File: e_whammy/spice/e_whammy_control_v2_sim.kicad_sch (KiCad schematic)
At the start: 29 parts, among them Q1 2N7002, U1 ${SIM.PARAMS}, U2 ${SIM.PARAMS}, U3 ADG779, U4 OPEN_COLLECTOR_COMPARATOR, U5 OPEN_COLLECTOR_COMPARATOR

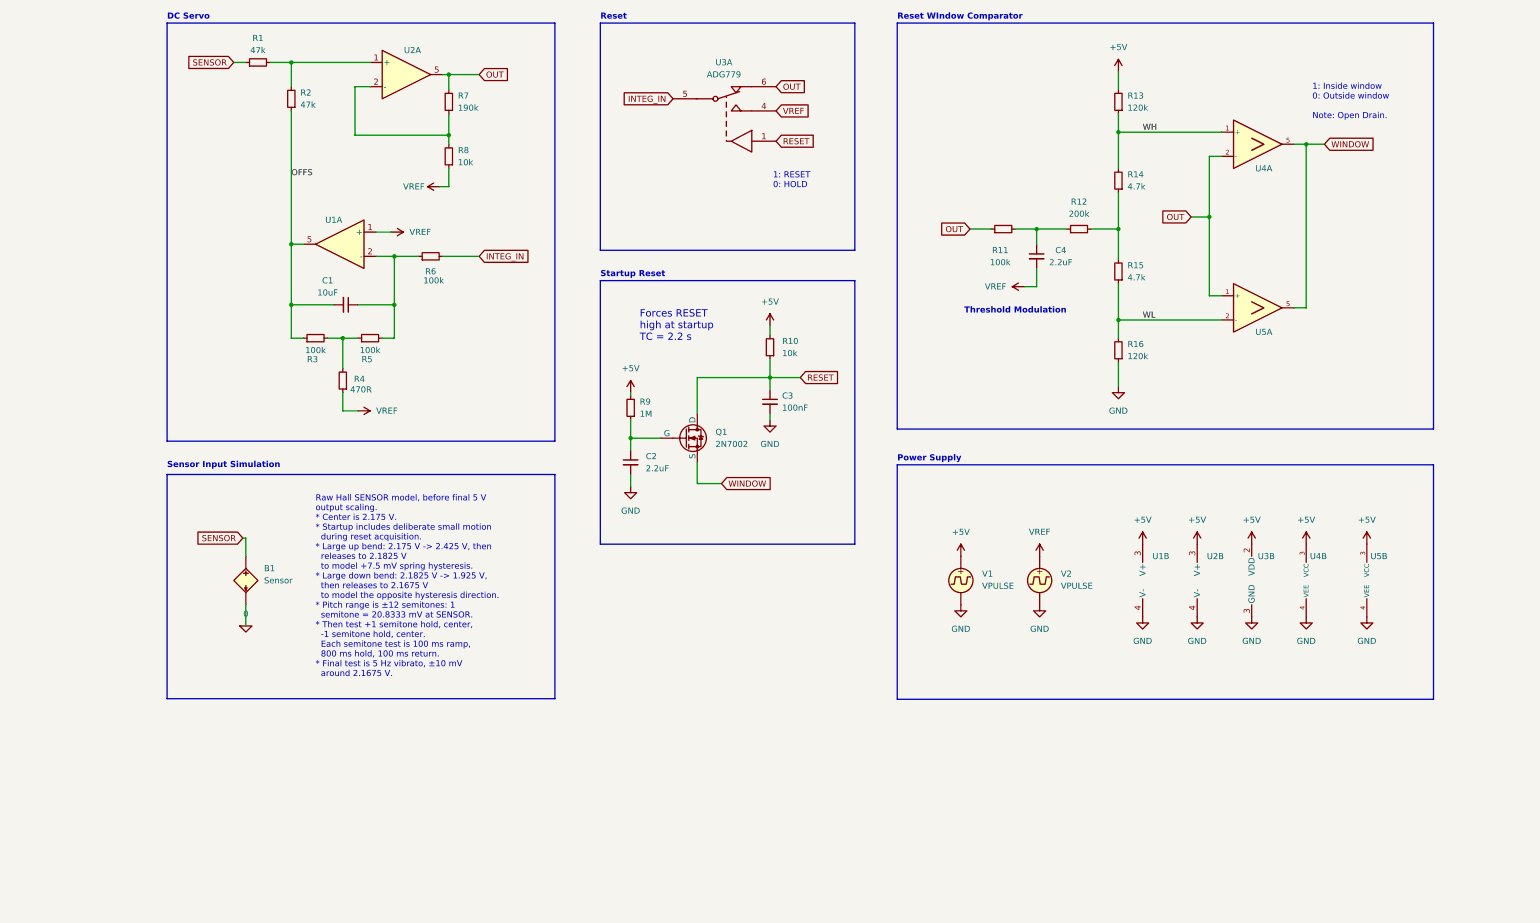
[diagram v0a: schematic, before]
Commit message: e-Whammy: add latch-up recovery to v2_sim (RESET = WINDOW OR STARTUP OR TIMEOUT)
Replaces Q1/R9/C2/R10/C3 startup-gate path with a 4-gate Schmitt-NAND
recovery: startup ramp + window comparators + asymmetric timeout envelope.
Bumps pcb_common for the SCHMITT_NAND symbol and cycfi_schmitt_nand subckt.
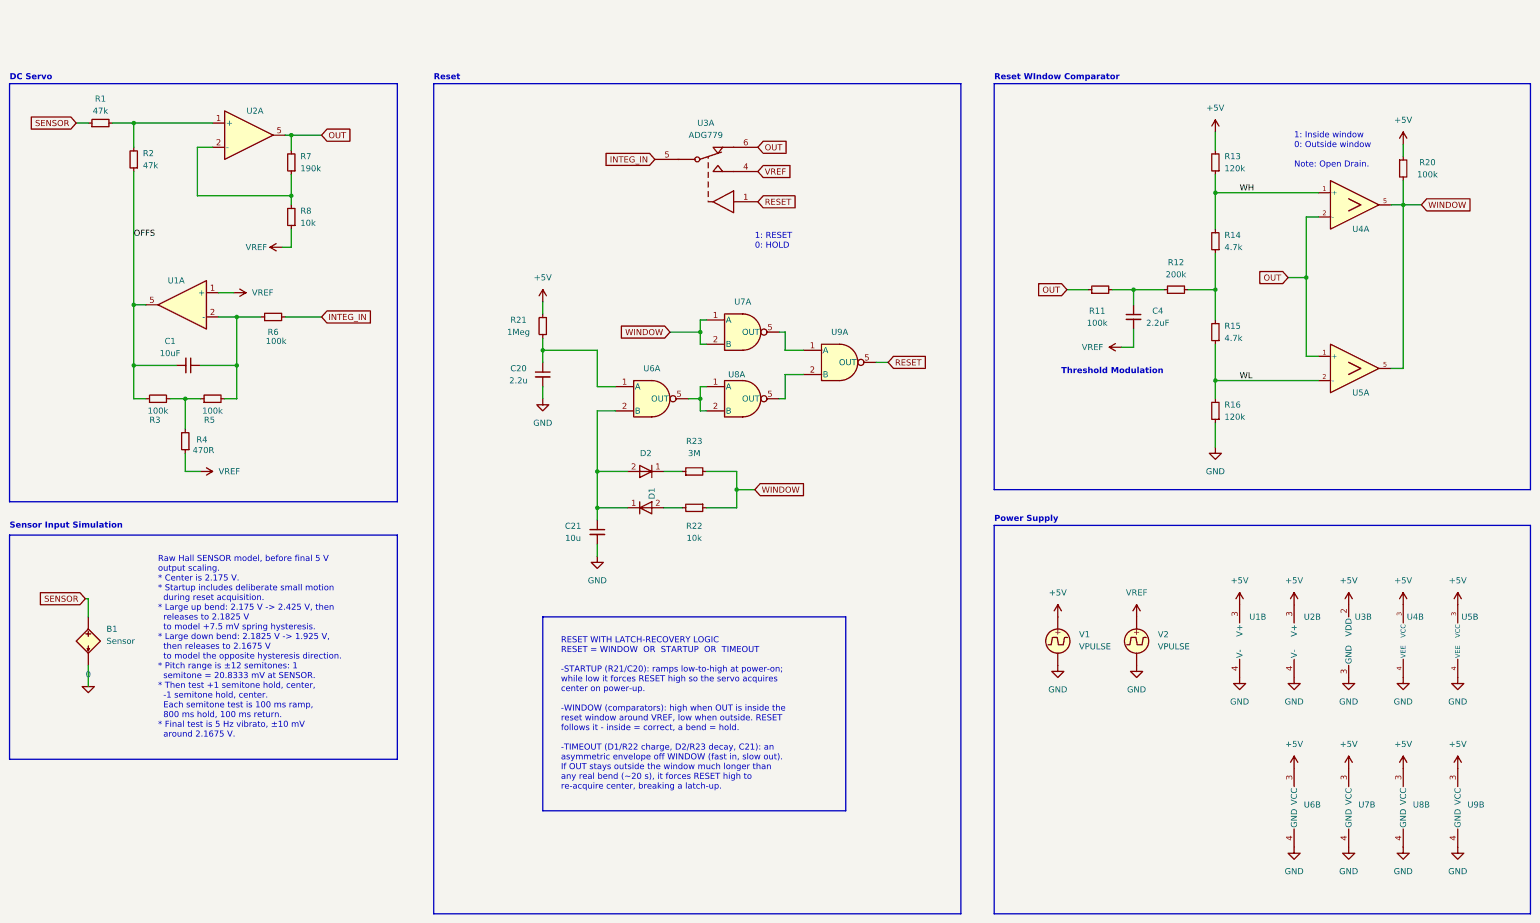
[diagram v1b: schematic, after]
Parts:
- removed C2: 2.2uF, symbol Device:C_Small
- removed C3: 100nF, symbol Device:C_Small
- removed Q1: 2N7002, symbol Simulation_SPICE:NMOS
- removed R10: 10k, symbol Device:R_Small
- removed R9: 1M, symbol Device:R_Small
- added C20: 2.2u, symbol Device:C_Small
- added C21: 10u, symbol Device:C_Small
- added D1, D2: D, symbol cycfi_spice_library:D
- added R20: 100k, symbol Device:R_Small
- added R21: 1Meg, symbol Device:R_Small
- added R22: 10k, symbol Device:R_Small
- added R23: 3M, symbol Device:R_Small
- added U6, U7, U8, U9: SCHMITT_NAND, symbol cycfi_spice_library:SCHMITT_NAND
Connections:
- net +5V: now also R20.1, R21.1, U6.3 (VCC), U7.3 (VCC), U8.3 (VCC), U9.3 (VCC)
- net GND: now also C20.2, C21.2, U6.4 (GND), U7.4 (GND), U8.4 (GND), U9.4 (GND)
- net RESET: now also U9.5 (OUT)
- net WINDOW: now also R20.2, R22.1, R23.2, U7.1 (A), U7.2 (B)
- new net: C21.1, D1.1 (K), D2.2 (A), U6.2 (B)
- new net: D1.2 (A), R22.2
- new net: U7.5 (OUT), U9.1 (A)
- new net: U8.5 (OUT), U9.2 (B)
- new net: D2.1 (K), R23.1
- new net: C20.1, R21.2, U6.1 (A)
- new net: U6.5 (OUT), U8.1 (A), U8.2 (B)
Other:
- note added: "RESET WITH LATCH-RECOVERY LOGIC RESET = WINDOW OR STARTUP OR TIMEOUT -STARTUP (R21/C20): ramps low-to-high at power-on; while low it forces RESET high so the servo acquires center on power-up. -WINDOW (comparators): high when OUT is inside the reset window around VREF, low when outside. RESET follows it - inside = correct, a bend = hold. -TIMEOUT (D1/R22 charge, D2/R23 decay, C21): an asymmetric 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"
- note removed: "Forces RESET high at startup TC = 2.2 s"
- note removed: "Startup Reset"
- moved on the sheet: B1, C1, C4, R1, R11, R12, R13, R14, R15, R16, R2, R3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

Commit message: e-Whammy: simplify latch recovery to 2 gates (NAND+NOR, active-low RESET)
Replaces the 4-NAND RESET=WINDOW OR STARTUP OR TIMEOUT with U6=NAND(startup,
timeout) -> U7=NOR(WINDOW,U6); ADG779 poles reversed so RESET is active-low
(0=correct, 1=hold). Deletes U7/U8/U9 (old NANDs). Full sim reproduces the
validated metrics. Bumps pcb_common for the SCHMITT_NOR symbol + subckt.
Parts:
- removed U7, U8, U9: SCHMITT_NAND, symbol cycfi_spice_library:SCHMITT_NAND
- added U7: SCHMITT_NOR, symbol cycfi_spice_library:SCHMITT_NOR
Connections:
- net +5V: now also U7.3 (VCC)
- net GND: now also U7.4 (GND)
- net OUT: now also U3.4; no longer U3.6
- net RESET: now also U7.5
- net VREF: now also U3.6; no longer U3.4
- net WINDOW: now also U7.1
- net at U6.5: now also U7.2
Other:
- note added: "0: RESET 1: HOLD"
- note added: "RESET WITH LATCH-RECOVERY LOGIC RESET = WINDOW OR STARTUP OR TIMEOUT (active-low: 0 = correct, 1 = hold) -STARTUP (R21/C20): ramps low-to-high at power-on; while low it pulls RESET low so the servo acquires center on power-up. -WINDOW (comparators): high when OUT is inside the reset window around VREF, low when outside; inside = correct, a bend = hold. -TIMEOUT (D1/R22 charge, D2/R23 decay, C21):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"
- note removed: "1: RESET 0: HOLD"
- note removed: "RESET WITH LATCH-RECOVERY LOGIC RESET = WINDOW OR STARTUP OR TIMEOUT -STARTUP (R21/C20): ramps low-to-high at power-on; while low it forces RESET high so the servo acquires center on power-up. -WINDOW (comparators): high when OUT is inside the reset window around VREF, low when outside. RESET follows it - inside = correct, a bend = hold. -TIMEOUT (D1/R22 charge, D2/R23 decay, C21): an asymmetric 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"
- moved on the sheet: C20, R21, U3A
